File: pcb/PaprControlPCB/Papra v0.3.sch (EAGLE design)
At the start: 32 parts, among them Q1 AO3400A (C20917), U1 LP2985-50DBVR (C74511), U2 ATTINYX04SOIC14

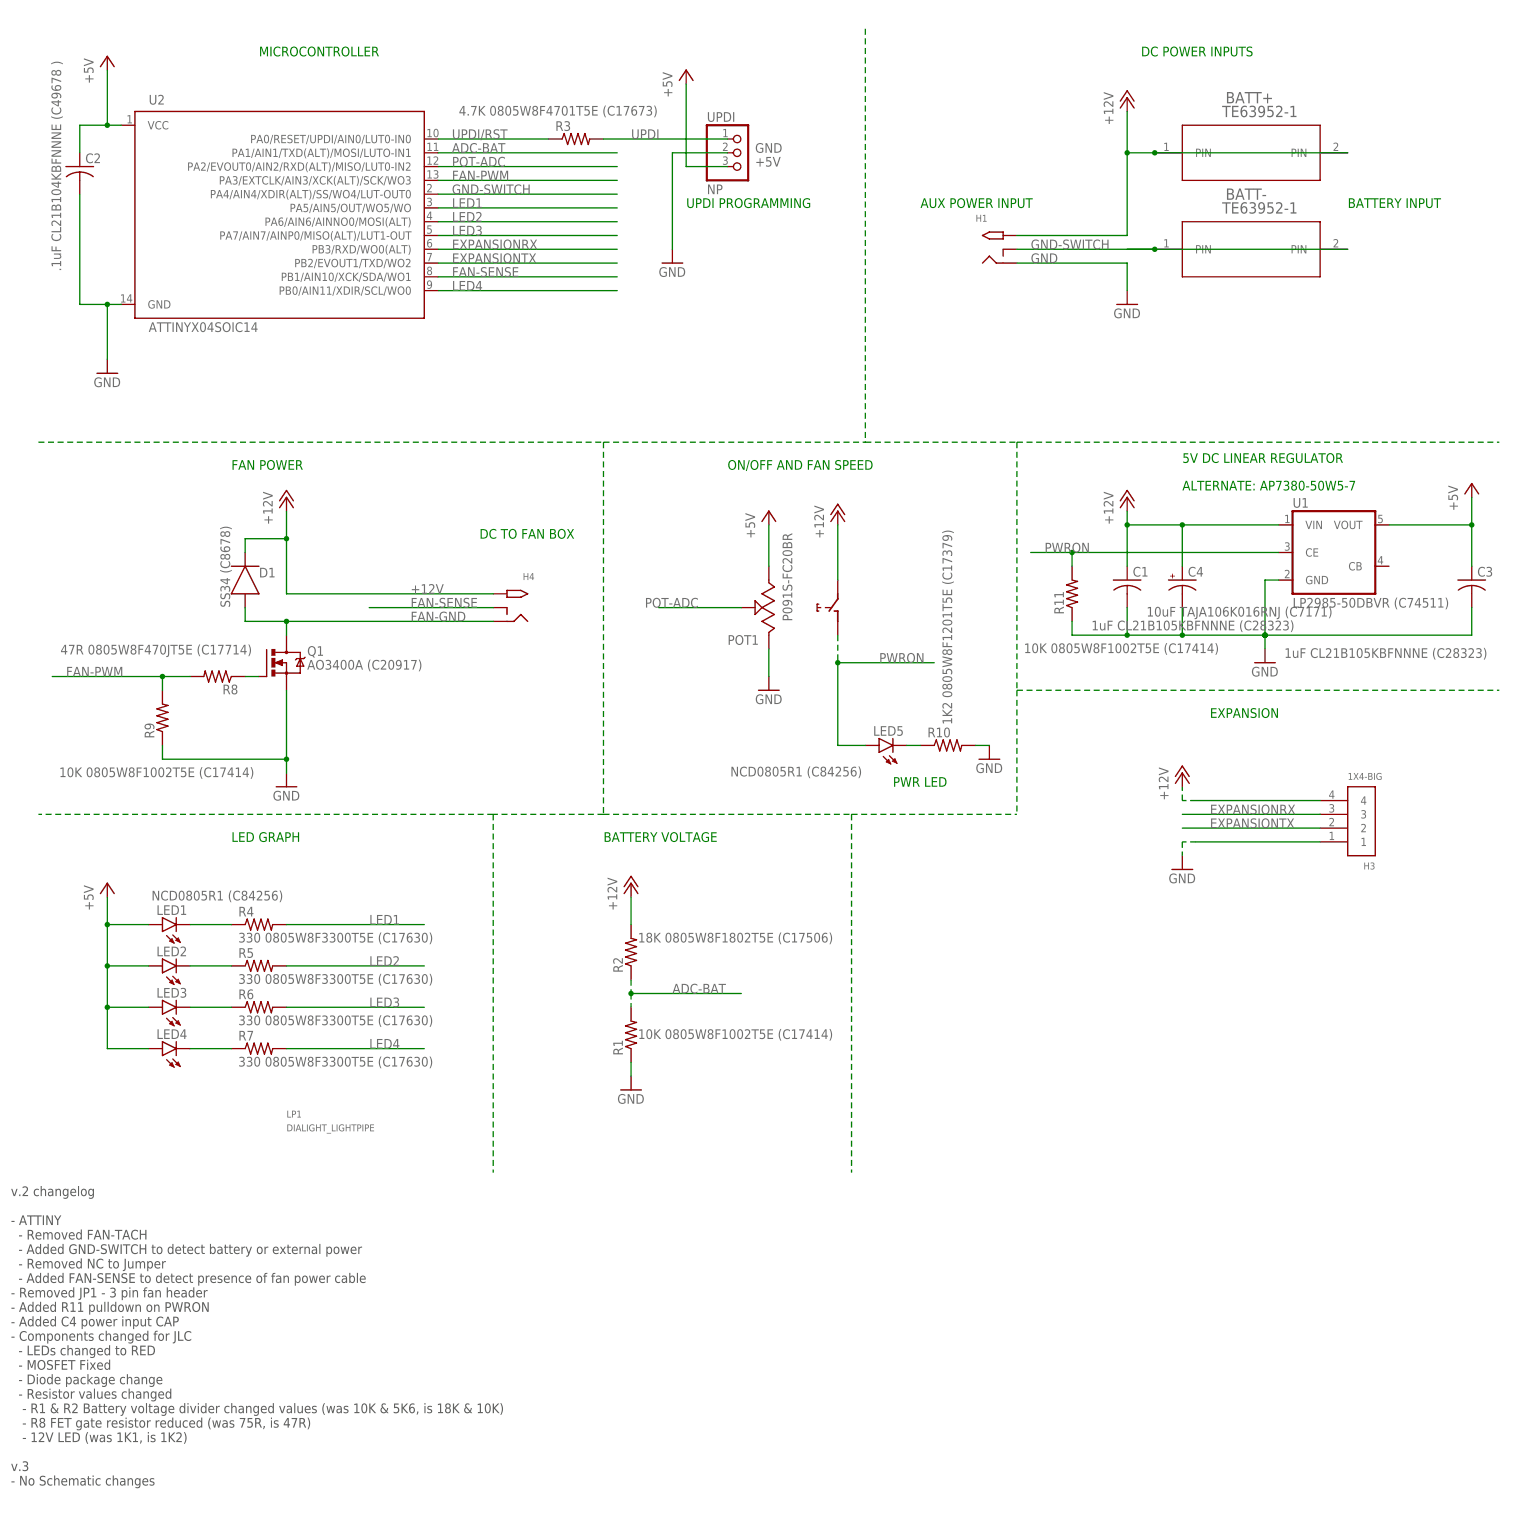
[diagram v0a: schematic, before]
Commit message: Added 1A resettable fuse to 12V power
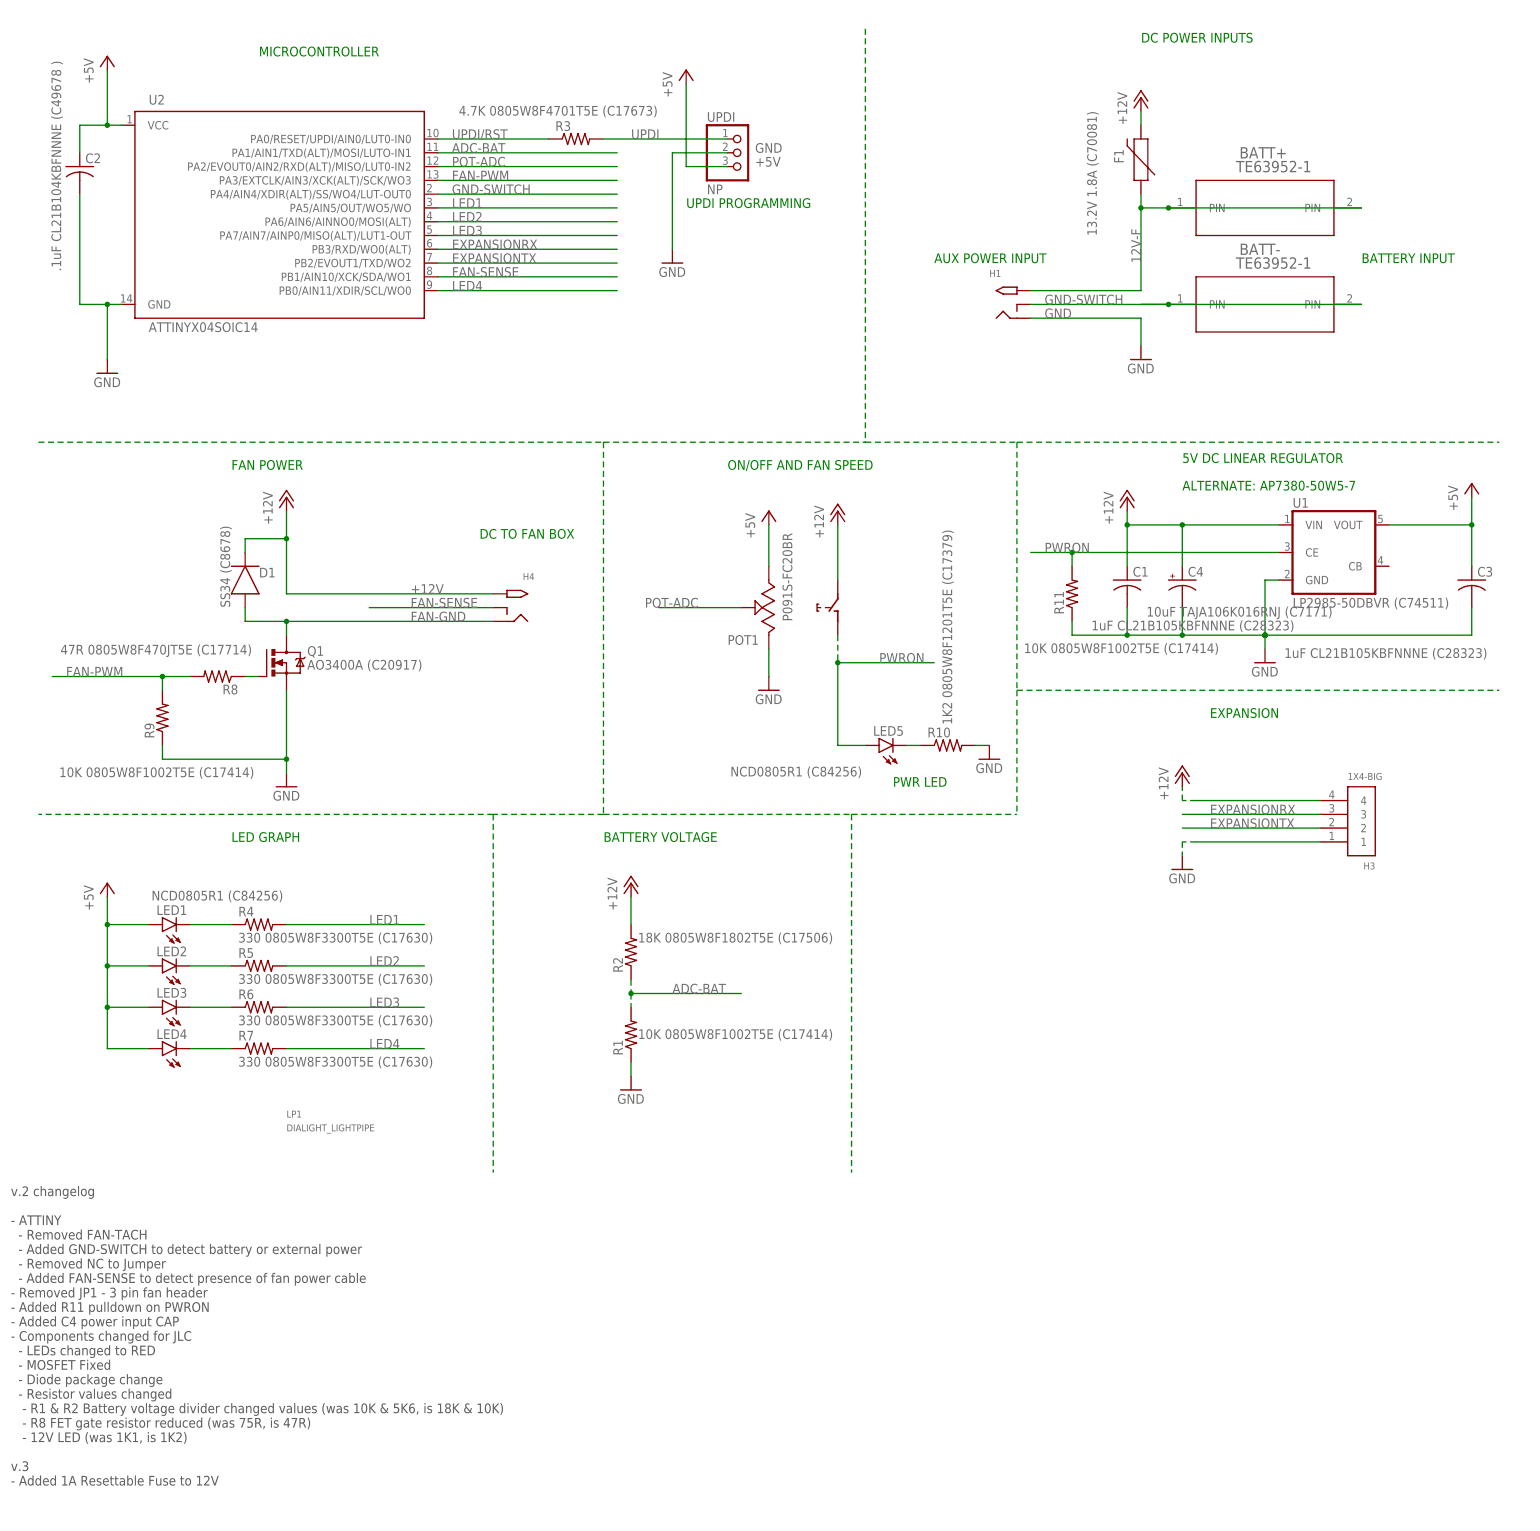
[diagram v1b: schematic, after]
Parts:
- added F1: 13.2V 1.8A (C70081), SparkFun-Fuses:PPTC_HALF-AMP
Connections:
- new net 12V-F: BATT+.PIN@1, BATT+.PIN@2, F1.1, H1.TIP
- net +12V: now also F1.2; no longer BATT+.PIN@1, BATT+.PIN@2, H1.TIP
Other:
- moved on the sheet: BATT+, BATT-, H1
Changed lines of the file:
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@@
 <part name="R11" library="rcl" library_urn="urn:adsk.eagle:library:334" deviceset="R-US_" device="R0805" package3d_urn="urn:adsk.eagle:package:23553/2" value="10K 0805W8F1002T5E (C17414)"/>
 <part name="C4" library="rcl" library_urn="urn:adsk.eagle:library:334" deviceset="CPOL-US" device="A/3216-18R" package3d_urn="urn:adsk.eagle:package:23410/2" value="10uF TAJA106K016RNJ (C7171)"/>
+<part name="F1" library="SparkFun-Fuses" library_urn="urn:adsk.eagle:library:517" deviceset="PPTC" device="_HALF-AMP" package3d_urn="urn:adsk.eagle:package:38575/1" value="13.2V 1.8A (C70081)"/>
 </parts>
 <sheets>
 <sheet>
 <plain>
-<text x="167.64" y="177.8" size="1.778" layer="91">AUX POWER INPUT</text>
-<text x="246.38" y="177.8" size="1.778" layer="91">BATTERY INPUT</text>
-<text x="208.28" y="205.74" size="1.778" layer="91">DC POWER INPUTS</text>
+<text x="170.18" y="167.64" size="1.778" layer="91">AUX POWER INPUT</text>
+<text x="248.92" y="167.64" size="1.778" layer="91">BATTERY INPUT</text>
+<text x="208.28" y="208.28" size="1.778" layer="91">DC POWER INPUTS</text>
 <text x="215.9" y="130.81" size="1.778" layer="91">5V DC LINEAR REGULATOR</text>
 <text x="132.08" y="129.54" size="1.778" layer="91">ON/OFF AND FAN SPEED</text>
@@
    - 12V LED (was 1K1, is 1K2)
 v.3
-- No Schematic changes</text>
+- Added 1A Resettable Fuse to 12V</text>
 </plain>
 <instances>
@@
 <attribute name="VALUE" x="15.24" y="144.78" size="1.778" layer="96"/>
 </instance>
-<instance part="BATT+" gate="G$1" x="228.6" y="187.96" smashed="yes">
-<attribute name="NAME" x="223.8756" y="197.0786" size="2.0828" layer="95" ratio="6" rot="SR0"/>
-<attribute name="VALUE" x="223.2406" y="194.5386" size="2.0828" layer="96" ratio="6" rot="SR0"/>
-</instance>
-<instance part="BATT-" gate="G$1" x="228.6" y="170.18" smashed="yes">
-<attribute name="NAME" x="223.8756" y="179.2986" size="2.0828" layer="95" ratio="6" rot="SR0"/>
-<attribute name="VALUE" x="223.2406" y="176.7586" size="2.0828" layer="96" ratio="6" rot="SR0"/>
-</instance>
-<instance part="GND2" gate="1" x="205.74" y="160.02" smashed="yes">
-<attribute name="VALUE" x="203.2" y="157.48" size="1.778" layer="96"/>
+<instance part="BATT+" gate="G$1" x="231.14" y="177.8" smashed="yes">
+<attribute name="NAME" x="226.4156" y="186.9186" size="2.0828" layer="95" ratio="6" rot="SR0"/>
+<attribute name="VALUE" x="225.7806" y="184.3786" size="2.0828" layer="96" ratio="6" rot="SR0"/>
+</instance>
+<instance part="BATT-" gate="G$1" x="231.14" y="160.02" smashed="yes">
+<attribute name="NAME" x="226.4156" y="169.1386" size="2.0828" layer="95" ratio="6" rot="SR0"/>
+<attribute name="VALUE" x="225.7806" y="166.5986" size="2.0828" layer="96" ratio="6" rot="SR0"/>
+</instance>
+<instance part="GND2" gate="1" x="208.28" y="149.86" smashed="yes">
+<attribute name="VALUE" x="205.74" y="147.32" size="1.778" layer="96"/>
 </instance>
 <instance part="P+2" gate="1" x="205.74" y="124.46" smashed="yes">
@@
 <attribute name="VALUE" x="40.4114" y="104.14" size="1.778" layer="96" rot="R90"/>
 </instance>
-<instance part="H1" gate="G$1" x="182.88" y="170.18" smashed="yes">
-<attribute name="NAME" x="177.8" y="175.26" size="1.27" layer="95"/>
+<instance part="H1" gate="G$1" x="185.42" y="160.02" smashed="yes">
+<attribute name="NAME" x="180.34" y="165.1" size="1.27" layer="95"/>
 </instance>
 <instance part="LED2" gate="G$1" x="27.94" y="38.1" smashed="yes" rot="R90">
@@
 <attribute name="VALUE" x="149.86" y="116.84" size="1.778" layer="96" rot="R90"/>
 </instance>
-<instance part="P+4" gate="1" x="205.74" y="198.12" smashed="yes">
-<attribute name="VALUE" x="203.2" y="193.04" size="1.778" layer="96" rot="R90"/>
+<instance part="P+4" gate="1" x="208.28" y="198.12" smashed="yes">
+<attribute name="VALUE" x="205.74" y="193.04" size="1.778" layer="96" rot="R90"/>
 </instance>
 <instance part="P+11" gate="1" x="215.9" y="73.66" smashed="yes">
@@
 <attribute name="NAME" x="216.916" y="109.855" size="1.778" layer="95"/>
 <attribute name="VALUE" x="209.296" y="102.489" size="1.778" layer="96"/>
+</instance>
+<instance part="F1" gate="G$1" x="208.28" y="185.42" smashed="yes" rot="R90">
+<attribute name="NAME" x="205.105" y="187.325" size="1.778" layer="95" font="vector" rot="R90" align="bottom-center"/>
+<attribute name="VALUE" x="198.374" y="184.15" size="1.778" layer="96" font="vector" rot="R90" align="top-center"/>
 </instance>
 </instances>
@@
 <pinref part="H1" gate="G$1" pin="RING"/>
 <pinref part="GND2" gate="1" pin="GND"/>
-<wire x1="185.42" y1="167.64" x2="205.74" y2="167.64" width="0.1524" layer="91"/>
-<wire x1="205.74" y1="167.64" x2="205.74" y2="162.56" width="0.1524" layer="91"/>
-<label x="187.96" y="167.64" size="1.778" layer="95"/>
+<wire x1="187.96" y1="157.48" x2="208.28" y2="157.48" width="0.1524" layer="91"/>
+<wire x1="208.28" y1="157.48" x2="208.28" y2="152.4" width="0.1524" layer="91"/>
+<label x="190.5" y="157.48" size="1.778" layer="95"/>
 </segment>
 <segment>
@@
 </segment>
 <segment>
-<pinref part="BATT+" gate="G$1" pin="PIN@2"/>
-<pinref part="BATT+" gate="G$1" pin="PIN@1"/>
-<wire x1="246.38" y1="187.96" x2="210.82" y2="187.96" width="0.1524" layer="91"/>
-<wire x1="210.82" y1="187.96" x2="205.74" y2="187.96" width="0.1524" layer="91"/>
-<wire x1="205.74" y1="187.96" x2="205.74" y2="195.58" width="0.1524" layer="91"/>
-<junction x="210.82" y="187.96"/>
-<pinref part="H1" gate="G$1" pin="TIP"/>
-<wire x1="185.42" y1="172.72" x2="205.74" y2="172.72" width="0.1524" layer="91"/>
-<wire x1="205.74" y1="172.72" x2="205.74" y2="187.96" width="0.1524" layer="91"/>
-<junction x="205.74" y="187.96"/>
-<pinref part="P+4" gate="1" pin="+12V"/>
-</segment>
-<segment>
 <wire x1="218.44" y1="68.58" x2="241.3" y2="68.58" width="0.1524" layer="91"/>
 <wire x1="218.44" y1="68.58" x2="215.9" y2="68.58" width="0.1524" layer="91" style="longdash"/>
@@
 <pinref part="P+1" gate="1" pin="+12V"/>
 <wire x1="152.4" y1="119.38" x2="152.4" y2="109.22" width="0.1524" layer="91"/>
+</segment>
+<segment>
+<pinref part="P+4" gate="1" pin="+12V"/>
+<pinref part="F1" gate="G$1" pin="2"/>
+<wire x1="208.28" y1="195.58" x2="208.28" y2="193.04" width="0.1524" layer="91"/>
 </segment>
 </net>
@@
 <segment>
 <pinref part="BATT-" gate="G$1" pin="PIN@1"/>
-<wire x1="205.74" y1="170.18" x2="210.82" y2="170.18" width="0.1524" layer="91"/>
+<wire x1="208.28" y1="160.02" x2="213.36" y2="160.02" width="0.1524" layer="91"/>
 <pinref part="BATT-" gate="G$1" pin="PIN@2"/>
-<wire x1="210.82" y1="170.18" x2="246.38" y2="170.18" width="0.1524" layer="91"/>
-<junction x="210.82" y="170.18"/>
+<wire x1="213.36" y1="160.02" x2="248.92" y2="160.02" width="0.1524" layer="91"/>
+<junction x="213.36" y="160.02"/>
 <pinref part="H1" gate="G$1" pin="RING_SW"/>
-<wire x1="185.42" y1="170.18" x2="210.82" y2="170.18" width="0.1524" layer="91"/>
-<label x="187.96" y="170.18" size="1.778" layer="95"/>
+<wire x1="187.96" y1="160.02" x2="213.36" y2="160.02" width="0.1524" layer="91"/>
+<label x="190.5" y="160.02" size="1.778" layer="95"/>
 </segment>
 <segment>
@@
 </segment>
 </net>
+<net name="12V-F" class="1">
+<segment>
+<pinref part="BATT+" gate="G$1" pin="PIN@2"/>
+<pinref part="BATT+" gate="G$1" pin="PIN@1"/>
+<wire x1="248.92" y1="177.8" x2="213.36" y2="177.8" width="0.1524" layer="91"/>
+<wire x1="213.36" y1="177.8" x2="208.28" y2="177.8" width="0.1524" layer="91"/>
+<junction x="213.36" y="177.8"/>
+<pinref part="H1" gate="G$1" pin="TIP"/>
+<wire x1="187.96" y1="162.56" x2="208.28" y2="162.56" width="0.1524" layer="91"/>
+<wire x1="208.28" y1="162.56" x2="208.28" y2="177.8" width="0.1524" layer="91"/>
+<pinref part="F1" gate="G$1" pin="1"/>
+<wire x1="208.28" y1="180.34" x2="208.28" y2="177.8" width="0.1524" layer="91"/>
+<junction x="208.28" y="177.8"/>
+<label x="208.28" y="167.64" size="1.778" layer="95" rot="R90"/>
+</segment>
+</net>
